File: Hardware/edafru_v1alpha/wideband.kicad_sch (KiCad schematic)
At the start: 42 parts, among them Q6 MMBT2222A, U13 LM324A, U15 CJ125, U16 CJ125

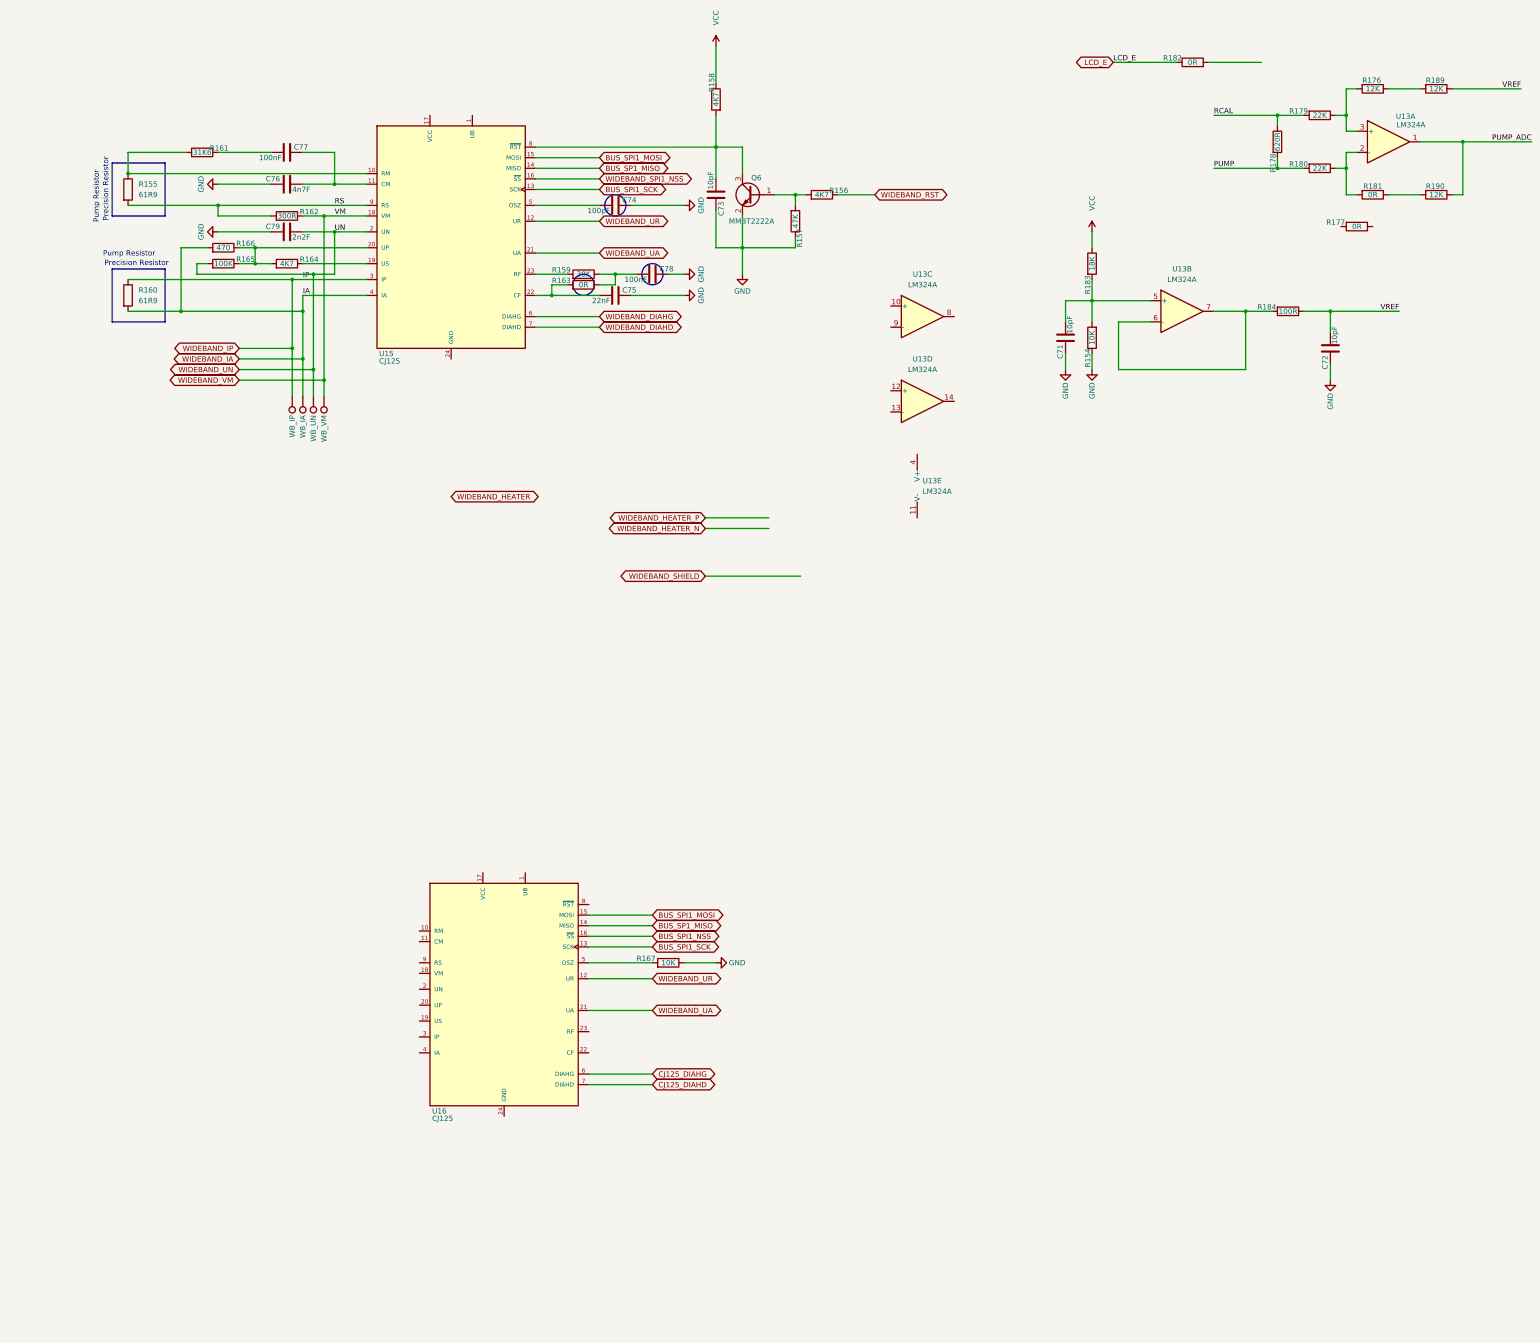
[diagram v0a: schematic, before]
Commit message: all need circuits included to the schematic. ready for pcb component placement.
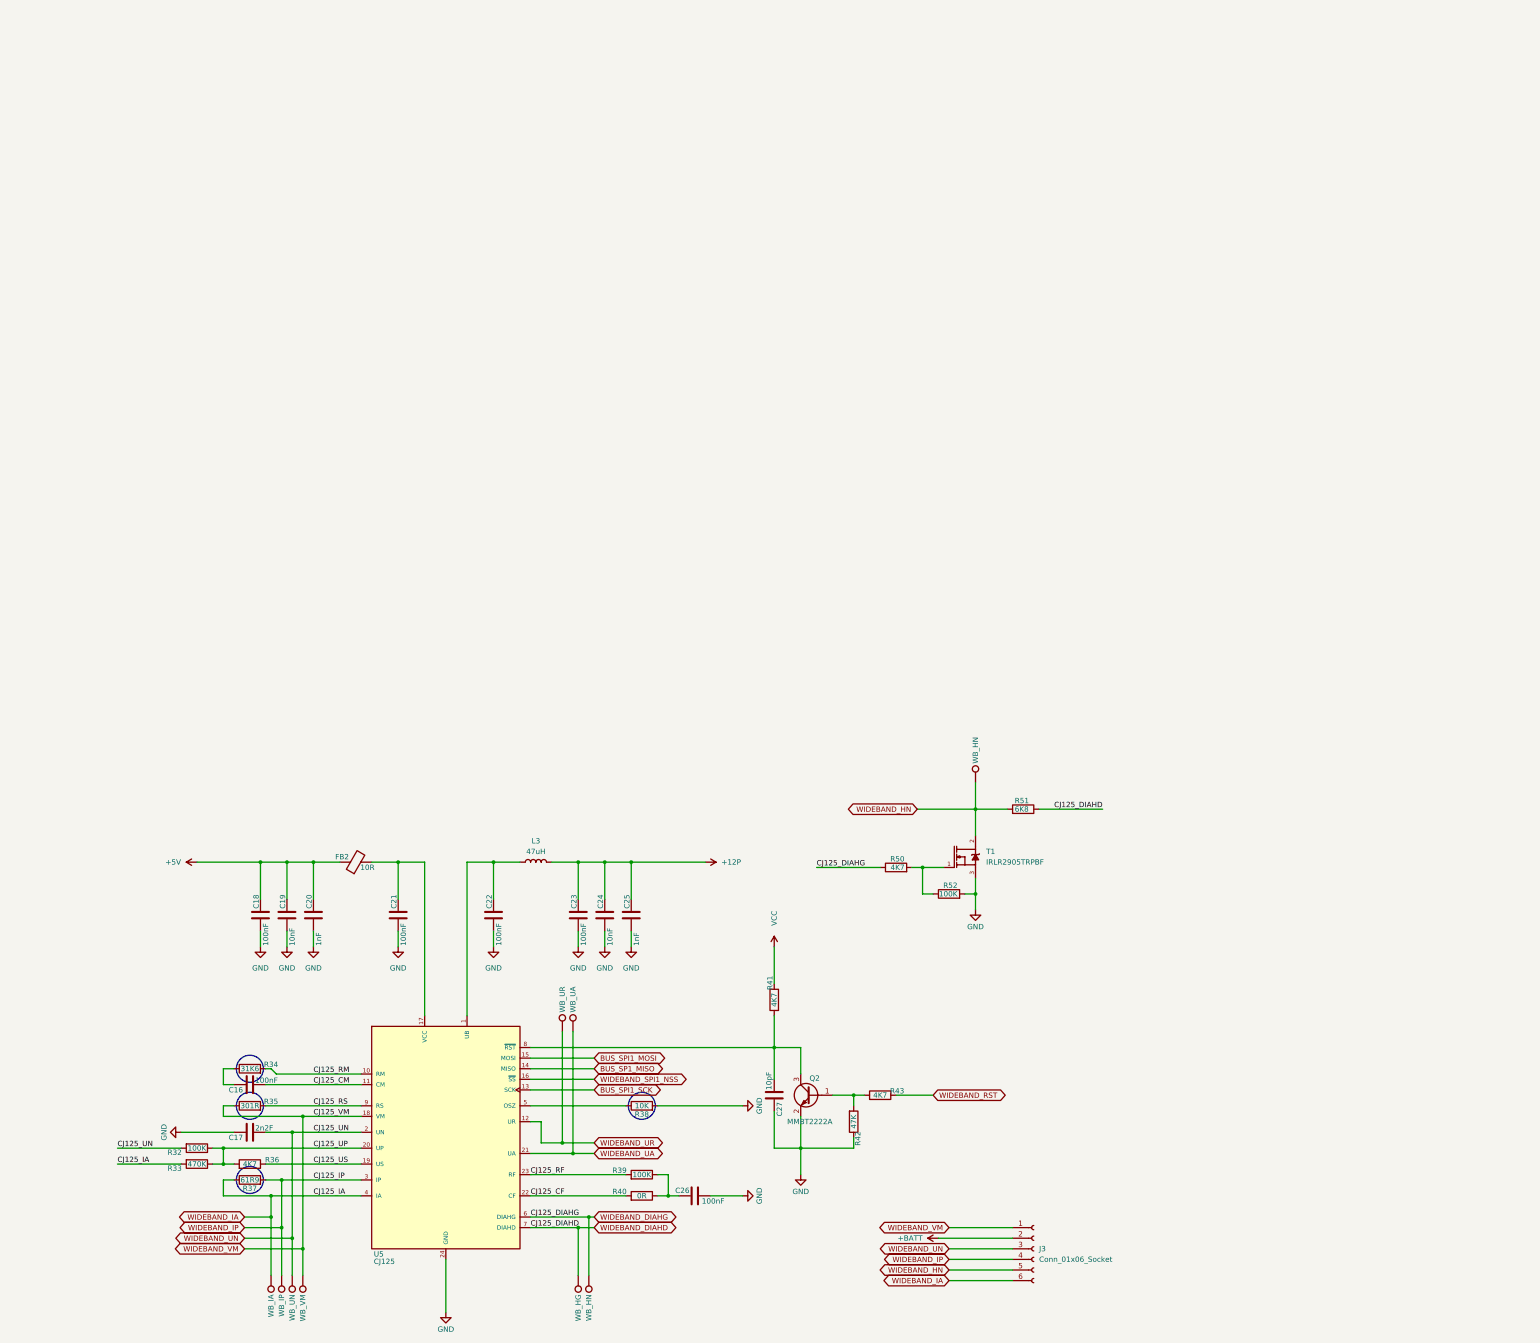
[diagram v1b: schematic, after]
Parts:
- removed C71, C72, C73: 10pF, Capacitor_SMD:C_0603_1608Metric_Pad1.08x0.95mm_HandSolder, symbol Device:C
- removed C74: 100pF, Capacitor_SMD:C_0603_1608Metric_Pad1.08x0.95mm_HandSolder, symbol Device:C
- removed C75: 22nF, Capacitor_SMD:C_0603_1608Metric_Pad1.08x0.95mm_HandSolder, symbol Device:C
- removed C76: 4n7F, Capacitor_SMD:C_0603_1608Metric_Pad1.08x0.95mm_HandSolder, symbol Device:C
- removed C77, C78: 100nF, Capacitor_SMD:C_0603_1608Metric_Pad1.08x0.95mm_HandSolder, symbol Device:C
- removed C79: 2n2F, Capacitor_SMD:C_0603_1608Metric_Pad1.08x0.95mm_HandSolder, symbol Device:C
- removed Q6: MMBT2222A, Package_TO_SOT_SMD:SOT-23, symbol Transistor_BJT:MMBT2222A
- removed R154, R167: 10K, Resistor_SMD:R_0603_1608Metric_Pad0.98x0.95mm_HandSolder, symbol Device:R
- removed R155, R160: 61R9, Resistor_SMD:R_MELF_MMB-0207, symbol Device:R
- removed R156, R158, R164: 4K7, Resistor_SMD:R_0603_1608Metric_Pad0.98x0.95mm_HandSolder, symbol Device:R
- removed R157: 47K, Resistor_SMD:R_0603_1608Metric_Pad0.98x0.95mm_HandSolder, symbol Device:R
- removed R159: 30K, Resistor_SMD:R_0603_1608Metric_Pad0.98x0.95mm_HandSolder, symbol Device:R
- removed R161: 31K6, Resistor_SMD:R_0603_1608Metric_Pad0.98x0.95mm_HandSolder, symbol Device:R
- removed R162: 300R, Resistor_SMD:R_0603_1608Metric_Pad0.98x0.95mm_HandSolder, symbol Device:R
- removed R163, R177, R181, R182: 0R, Resistor_SMD:R_0603_1608Metric_Pad0.98x0.95mm_HandSolder, symbol Device:R
- removed R165: 100K, Resistor_SMD:R_0603_1608Metric_Pad0.98x0.95mm_HandSolder, symbol Device:R
- removed R166: 470, Resistor_SMD:R_0603_1608Metric_Pad0.98x0.95mm_HandSolder, symbol Device:R
- removed R176, R189, R190: 12K, Resistor_SMD:R_0603_1608Metric_Pad0.98x0.95mm_HandSolder, symbol Device:R
- removed R178: 620R, Resistor_SMD:R_0603_1608Metric_Pad0.98x0.95mm_HandSolder, symbol Device:R
- removed R179, R180: 22K, Resistor_SMD:R_0603_1608Metric_Pad0.98x0.95mm_HandSolder, symbol Device:R
- removed R183: 18K, Resistor_SMD:R_0603_1608Metric_Pad0.98x0.95mm_HandSolder, symbol Device:R
- removed R184: 100R, Resistor_SMD:R_0603_1608Metric_Pad0.98x0.95mm_HandSolder, symbol Device:R
- removed TP10: WB_IP, TestPoint:TestPoint_Pad_D1.0mm, symbol Connector:TestPoint
- removed TP11: WB_UN, TestPoint:TestPoint_Pad_D1.0mm, symbol Connector:TestPoint
- removed TP12: WB_VM, TestPoint:TestPoint_Pad_D1.0mm, symbol Connector:TestPoint
- removed U13: LM324A, Package_SO:SOIC-14_3.9x8.7mm_P1.27mm, symbol Amplifier_Operational:LM324A
- removed U15, U16: CJ125, CJ125:SO24W, symbol CJ125:CJ125
- added C16, C26: 100nF, Capacitor_SMD:C_0603_1608Metric_Pad1.08x0.95mm_HandSolder, symbol Device:C
- added C17: 2n2F, Capacitor_SMD:C_0603_1608Metric_Pad1.08x0.95mm_HandSolder, symbol Device:C
- added C18, C21, C22, C23: 100nF, Capacitor_SMD:C_1206_3216Metric_Pad1.33x1.80mm_HandSolder, symbol Device:C
- added C19, C24: 10nF, Capacitor_SMD:C_1206_3216Metric_Pad1.33x1.80mm_HandSolder, symbol Device:C
- added C20, C25: 1nF, Capacitor_SMD:C_1206_3216Metric_Pad1.33x1.80mm_HandSolder, symbol Device:C
- added C27: 10pF, Capacitor_SMD:C_0603_1608Metric_Pad1.08x0.95mm_HandSolder, symbol Device:C
- added FB2: 10R, Inductor_SMD:L_1206_3216Metric_Pad1.22x1.90mm_HandSolder, symbol Device:FerriteBead
- added J3: Conn_01x06_Socket, Connector_Molex:Molex_KK-254_AE-6410-06A_1x06_P2.54mm_Vertical, symbol Connector:Conn_01x06_Socket
- added L3: 47uH, Inductor_SMD:L_1210_3225Metric_Pad1.42x2.65mm_HandSolder, symbol Device:L
- added Q2: MMBT2222A, Package_TO_SOT_SMD:SOT-23, symbol Transistor_BJT:MMBT2222A
- added R32, R39: 100K, Resistor_SMD:R_0603_1608Metric_Pad0.98x0.95mm_HandSolder, symbol Device:R
- added R33: 470K, Resistor_SMD:R_0603_1608Metric_Pad0.98x0.95mm_HandSolder, symbol Device:R
- added R34: 31K6, Resistor_SMD:R_MELF_MMB-0207, symbol Device:R
- added R35: 301R, Resistor_SMD:R_MELF_MMB-0207, symbol Device:R
- added R36, R41, R43: 4K7, Resistor_SMD:R_0603_1608Metric_Pad0.98x0.95mm_HandSolder, symbol Device:R
- added R37: 61R9, Resistor_SMD:R_MELF_MMB-0207, symbol Device:R
- added R38: 10K, Resistor_SMD:R_MELF_MMB-0207, symbol Device:R
- added R40: 0R, Resistor_SMD:R_0603_1608Metric_Pad0.98x0.95mm_HandSolder, symbol Device:R
- added R42: 47K, Resistor_SMD:R_0603_1608Metric_Pad0.98x0.95mm_HandSolder, symbol Device:R
- added R50: 4K7, Resistor_SMD:R_1206_3216Metric_Pad1.30x1.75mm_HandSolder, symbol Device:R
- added R51: 6K8, Resistor_SMD:R_1206_3216Metric_Pad1.30x1.75mm_HandSolder, symbol Device:R
- added R52: 100K, Resistor_SMD:R_1206_3216Metric_Pad1.30x1.75mm_HandSolder, symbol Device:R
- added T1: IRLR2905TRPBF, ~edafru_v1alpha.kicad_pro:IRLR2905TRPBF, symbol IRLR2905TRPBF:IRLR2905TRPBF
- added TP1: WB_UR, TestPoint:TestPoint_Pad_D1.0mm, symbol Connector:TestPoint
- added TP2: WB_UA, TestPoint:TestPoint_Pad_D1.0mm, symbol Connector:TestPoint
- added TP3: WB_IP, TestPoint:TestPoint_Pad_D1.0mm, symbol Connector:TestPoint
- added TP4: WB_IA, TestPoint:TestPoint_Pad_D1.0mm, symbol Connector:TestPoint
- added TP5: WB_UN, TestPoint:TestPoint_Pad_D1.0mm, symbol Connector:TestPoint
- added TP6: WB_VM, TestPoint:TestPoint_Pad_D1.0mm, symbol Connector:TestPoint
- added TP7: WB_HN, TestPoint:TestPoint_Pad_D1.0mm, symbol Connector:TestPoint
- added TP8: WB_HG, TestPoint:TestPoint_Pad_D1.0mm, symbol Connector:TestPoint
- added U5: CJ125, ~edafru_v1alpha.kicad_pro:CJ125, symbol CJ125:CJ125
- TP9: value WB_IA -> WB_HN
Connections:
- net BUS_SP1_MISO: now also U5.14 (MISO)
- net BUS_SPI1_MOSI: now also U5.15 (MOSI)
- net BUS_SPI1_SCK: now also U5.13 (SCK)
- net GND: now also C17.2, C18.2, C19.2, C20.2, C21.2, C22.2, C23.2, C24.2, C25.2, C26.2, C27.2, Q2.2 (E), R38.2, R42.1, R52.2, T1.3, U5.24 (GND)
- net VCC: now also R41.1
- net WIDEBAND_DIAHD: now also R51.1, TP8.1, U5.7 (DIAHD)
- net WIDEBAND_DIAHG: now also TP9.1, R50.1, U5.6 (DIAHG)
- net WIDEBAND_IA: now also J3.6 (Pin_6), R33.2, R37.1, TP4.1, U5.4 (IA); no longer TP9.1
- net WIDEBAND_IP: now also J3.4 (Pin_4), R37.2, TP3.1, U5.3 (IP)
- net WIDEBAND_RST: now also R43.1
- net WIDEBAND_SPI1_NSS: now also U5.16 (~{SS})
- net WIDEBAND_UA: now also TP2.1, U5.21 (UA)
- net WIDEBAND_UN: now also C17.1, J3.3 (Pin_3), R32.2, TP5.1, U5.2 (UN)
- net WIDEBAND_UR: now also TP1.1, U5.12 (UR)
- net WIDEBAND_VM: now also J3.1 (Pin_1), R35.1, TP6.1, U5.18 (VM)
- new net: R50.2, R52.1, T1.1
- new net: C26.1, R39.1, R40.1
- new net: Q2.1 (B), R42.2, R43.2
- new net: C22.1, L3.1, U5.1 (UB)
- new net: C27.1, Q2.3 (C), R41.2, U5.8 (~{RST})
- new net: C21.1, FB2.2, U5.17 (VCC)
- new net: R38.1, U5.5 (OSZ)
- new net: C16.2, R34.1
- new net +12P: C23.1, C24.1, C25.1, L3.2
- new net +5V: C18.1, C19.1, C20.1, FB2.1
- new net +BATT: J3.2 (Pin_2)
- new net CJ125_CF: R40.2, U5.22 (CF)
- new net CJ125_CM: C16.1, U5.11 (CM)
- new net CJ125_RF: R39.2, U5.23 (RF)
- new net CJ125_RM: R34.2, U5.10 (RM)
- new net CJ125_RS: R35.2, U5.9 (RS)
- new net CJ125_UP: R32.1, R33.1, R36.2, U5.20 (UP)
- new net CJ125_US: R36.1, U5.19 (US)
- new net WIDEBAND_HN: J3.5 (Pin_5), R51.2, T1.2, T1.PAD, TP7.1
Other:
- note removed: "Precision Resistor"
- note removed: "Pump Resistor"

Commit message: PCB is developing...
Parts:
- U5: footprint ~edafru_v1alpha.kicad_pro:CJ125 -> Package_SO:SOIC-24W_7.5x15.4mm_P1.27mm
- renumbered J3 to J4, Q2 to Q1, R32 to R34, R33 to R35, R34 to R36, R35 to R37, R36 to R38, R37 to R39, R38 to R40, R39 to R41, R40 to R42, R41 to R43, R42 to R44, R43 to R45, R50 to R46, R52 to R47, R51 to R48, TP4 to TP1, TP3 to TP2, TP5 to TP3, TP6 to TP4, TP1 to TP5, TP2 to TP6, TP8 to TP7, TP9 to TP8, TP7 to TP9

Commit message: developement is stopped depend on new EDVDU.
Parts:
- J4: value Conn_01x06_Socket -> WIDEBAND SENSOR
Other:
- note added: "WIDEBAND"
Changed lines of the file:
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@@
 		)
 	)
+	(rectangle
+		(start 246.38 137.16)
+		(end 260.35 158.75)
+		(stroke
+			(width 0)
+			(type default)
+		)
+		(fill
+			(type none)
+		)
+	)
 	(circle
 		(center 66.04 104.14)
@@
 		)
 	)
+	(text "WIDEBAND"
+		(exclude_from_sim no)
+		(at 65.278 26.67 0)
+		(effects
+			(font
+				(size 12.7 12.7)
+				(color 0 0 255 1)
+			)
+		)
+	)
 	(junction
 		(at 144.78 54.61)
@@
 		(at 240.03 41.91)
 		(diameter 0)
-		(color 0 0 0 0)
+		(color 0 132 0 1)
 	)
 	(junction
@@
 			(width 0)
 			(type default)
-			(color 0 255 255 1)
+			(color 0 194 194 1)
 		)
 	)
@@
 			(width 0)
 			(type default)
+			(color 0 132 0 1)
 		)
 	)
@@
 			(width 0)
 			(type default)
+			(color 0 132 0 1)
 		)
 	)
@@
 			(width 0)
 			(type default)
+			(color 0 132 0 1)
 		)
 	)
@@
 			(width 0)
 			(type default)
+			(color 0 132 0 1)
 		)
 	)
@@
 			(font
 				(size 1.27 1.27)
+				(color 132 0 0 1)
 			)
 			(justify right)
@@
 			(font
 				(size 1.27 1.27)
+				(color 132 0 0 1)
 			)
 			(justify right)
@@
 		(in_pos_files yes)
 		(dnp no)
-		(fields_autoplaced yes)
 		(property "Reference" "J4"
 			(at 255.27 147.3199 0)
+			(hide yes)
 			(show_name no)
 			(do_not_autoplace no)
@@
 			)
 		)
-		(property "Value" "Conn_01x06_Socket"
-			(at 255.27 149.8599 0)
+		(property "Value" "WIDEBAND SENSOR"
+			(at 256.032 156.972 90)
 			(show_name no)
 			(do_not_autoplace no)
